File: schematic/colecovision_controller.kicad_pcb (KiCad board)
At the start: 2 copper layers, 112.4 x 59.1 mm, 56 parts, among them J1 Conn_01x09, SW1 SW_AST, SW10 SW_9, SW11 SW_6, SW12 SW_3, SW13 SW_LEFT, SW14 SW_UP, SW15 SW_DOWN, SW16 SW_RIGHT, SW17 SW_ARM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

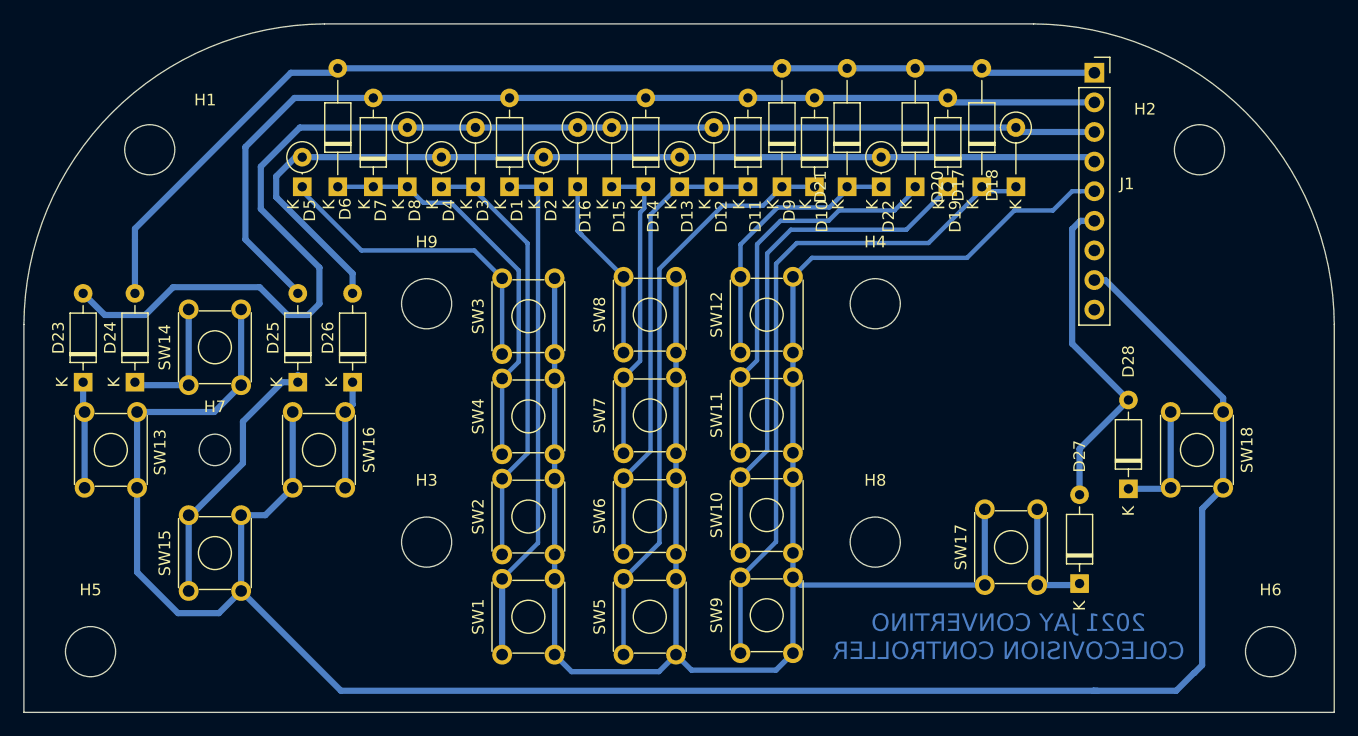
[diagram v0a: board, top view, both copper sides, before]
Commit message: updated to fix arm/fire button position. Now matches original controller.
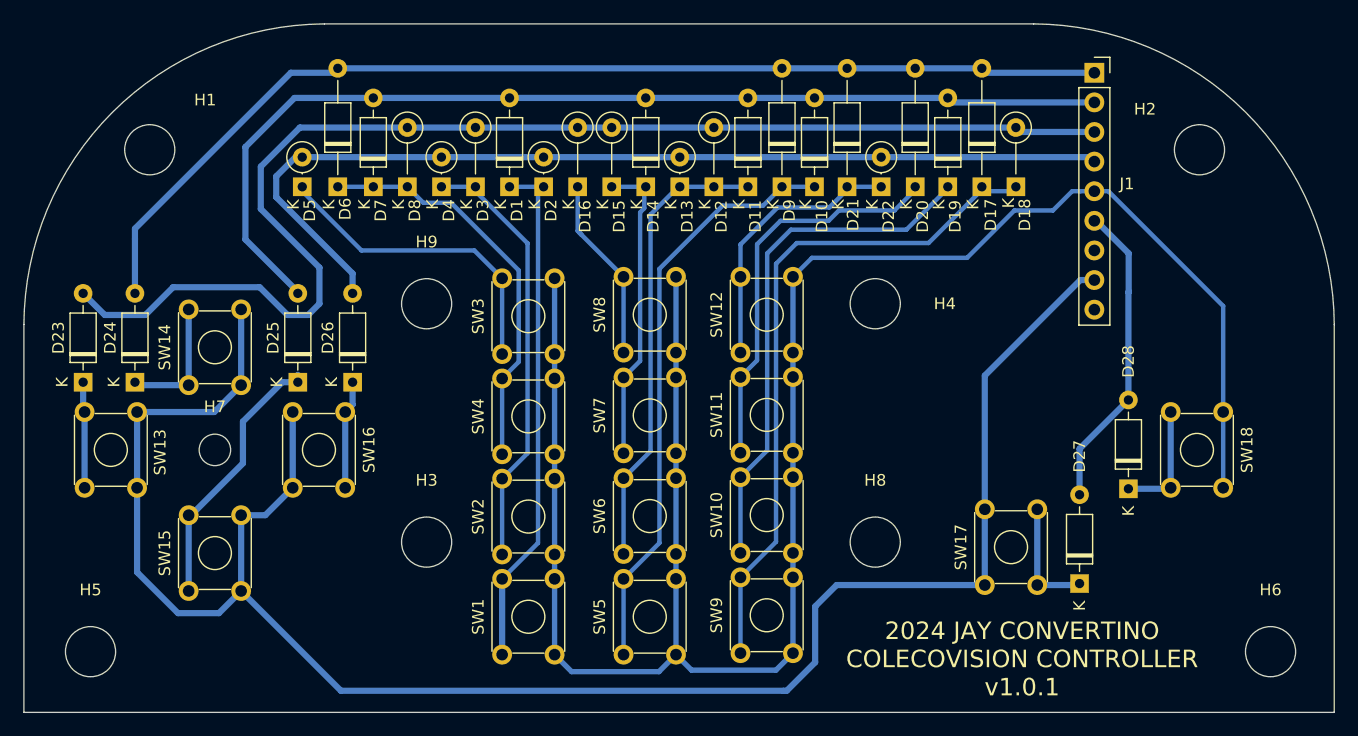
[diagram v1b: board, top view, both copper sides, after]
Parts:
- SW17: value SW_ARM -> SW_FIRE
- SW18: value SW_FIRE -> SW_ARM
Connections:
- J1 pad 7: Net-(J1-Pad7) -> unconnected-(J1-Pin_7-Pad7)
- J1 pad 9: Net-(J1-Pad9) -> unconnected-(J1-Pin_9-Pad9)
- SW17 pad 1: /DIN_5 -> /DIN_8
- SW17 pad 2: /DIN_5 -> /DIN_8
- SW18 pad 1: /DIN_8 -> /DIN_5
- SW18 pad 2: /DIN_8 -> /DIN_5
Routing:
- net /DIN_8: track 186.5 -> 165.0 mm
- net /DIN_5: track 171.9 -> 179.4 mm
- net /DIN_6: track 28.7 -> 26.6 mm
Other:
- board text added: "2024 JAY CONVERTINO COLECOVISION CONTROLLER v1.0.1"
- board text removed: "2021 JAY CONVERTINO COLECOVISION CONTROLLER"
